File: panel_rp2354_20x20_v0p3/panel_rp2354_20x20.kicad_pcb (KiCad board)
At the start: 6 copper layers, 45 x 45 mm, 557 parts, among them J1 Conn_01x04, J2 Conn_01x05, J3 Conn_01x05, J4 Conn_01x05, J5 Conn_01x05, SW1 SW_Push, SW2 SW_Push, U1 APS6404L-3SQR, U10 UCC27517, U11 UCC27517, U12 UCC27517, U13 UCC27517, U14 UCC27517, U15 UCC27517, U16 UCC27517, U17 UCC27517, U18 UCC27517, U19 UCC27517, U2 RP2354B_80QFN, U20 UCC27517, U21 UCC27517, U22 UCC27517, U23 UCC27517, U24 UCC27517, U25 UCC27517, U26 UCC27517, U27 UCC27517, U28 UCC27517, U29 UCC27517, U3 UCC27517, U30 UCC27517, U31 UCC27517, U32 UCC27517, U33 UCC27517, U34 UCC27517, U35 UCC27517, U36 UCC27517, U37 UCC27517, U38 UCC27517, U39 UCC27517, U4 UCC27517, U40 UCC27517, U41 UCC27517, U42 UCC27517, U43 AP2112K-3.3, U5 UCC27517, U6 UCC27517, U7 UCC27517, U8 UCC27517, U9 UCC27517, Y1 ABM8-272-T3

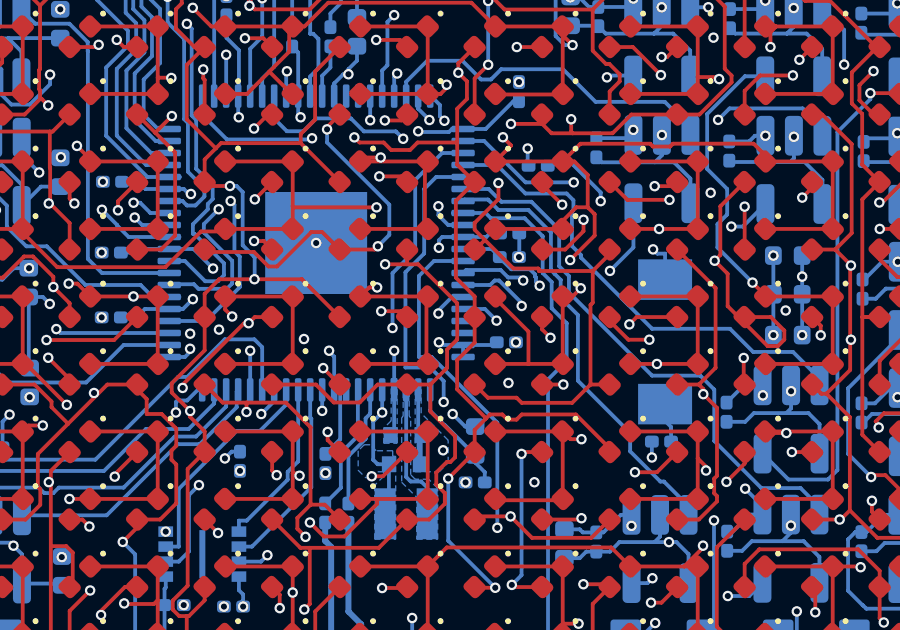
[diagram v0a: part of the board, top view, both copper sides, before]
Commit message: fix XIP_CS1n pind
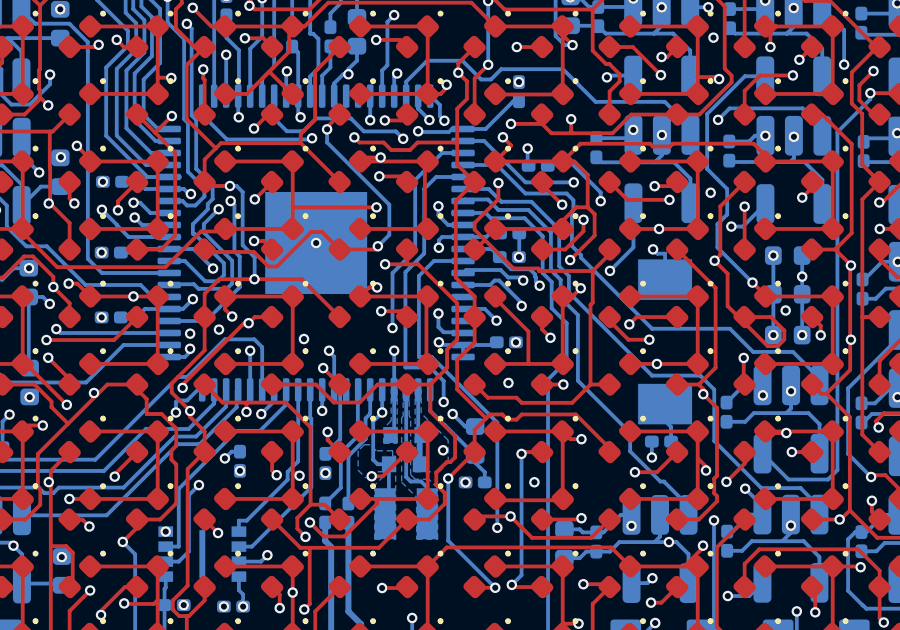
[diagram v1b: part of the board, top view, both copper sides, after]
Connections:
- U2 pad 55: /panel_mcu/XIP_CS1n -> unconnected-(U2-GPIO44_ADC4-Pad55)
- U2 pad 58: unconnected-(U2-GPIO47_ADC7-Pad58) -> /panel_mcu/XIP_CS1n
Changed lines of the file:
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@@
 		(title "G6 panel 45mm RP2354")
 		(date "2026-04-09")
-		(rev "v0.3.0")
+		(rev "v0.3.1")
 		(company "IORodeo for Reiserlab @ Janelia")
 	)
@@
 	(net 96 "/drivers/COL_MCU_17")
 	(net 97 "/drivers/COL_MCU_11")
-	(net 98 "unconnected-(U2-GPIO47_ADC7-Pad58)")
+	(net 98 "unconnected-(U2-GPIO44_ADC4-Pad55)")
 	(net 99 "/drivers/COL_MCU_02")
 	(net 100 "/drivers/ROW_MCU_11")
@@
 			(layers "B.Cu" "B.Mask" "B.Paste")
 			(roundrect_rratio 0.25)
-			(net 56 "/panel_mcu/XIP_CS1n")
+			(net 98 "unconnected-(U2-GPIO44_ADC4-Pad55)")
 			(pinfunction "GPIO44_ADC4")
-			(pintype "bidirectional")
+			(pintype "bidirectional+no_connect")
 			(thermal_bridge_angle 45)
 		)
@@
 			(layers "B.Cu" "B.Mask" "B.Paste")
 			(roundrect_rratio 0.25)
-			(net 98 "unconnected-(U2-GPIO47_ADC7-Pad58)")
+			(net 56 "/panel_mcu/XIP_CS1n")
 			(pinfunction "GPIO47_ADC7")
-			(pintype "bidirectional+no_connect")
+			(pintype "bidirectional")
 			(thermal_bridge_angle 45)
 		)
@@
 	)
 	(segment
+		(start 76.75 78.975)
+		(end 77.3715 78.975)
+		(width 0.127)
+		(layer "B.Cu")
+		(net 56)
+	)
+	(segment
 		(start 67.445 88.07)
 		(end 67.445 89.37)
@@
 	)
 	(segment
-		(start 76.575 78.35)
-		(end 76.575 78.475)
+		(start 77.3715 78.975)
+		(end 77.3965 79)
 		(width 0.127)
 		(layer "B.Cu")
@@
 	)
 	(segment
-		(start 77.025 77.8)
-		(end 76.525 78.3)
+		(start 67.445 87.5252)
+		(end 67.445 88.07)
 		(width 0.127)
 		(layer "B.Cu")
@@
 	)
 	(segment
-		(start 67.445 87.5252)
-		(end 67.445 88.07)
+		(start 76.575 78.35)
+		(end 76.575 78.8)
 		(width 0.127)
 		(layer "B.Cu")
@@
 	)
 	(segment
-		(start 77.3965 77.8)
-		(end 77.025 77.8)
+		(start 76.575 78.8)
+		(end 76.75 78.975)
 		(width 0.127)
 		(layer "B.Cu")
